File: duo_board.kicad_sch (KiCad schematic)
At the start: 24 parts, among them J1 TRRS, J2 2171790001, J3 Conn_01x04_Pin, U1 STM32F103C8Tx, U3 AMS1117-3.3, Y1 16Mhz

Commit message: routed, ready for production?
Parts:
- C1, C2, C3, C4, C8: value 100n -> 100nF; footprint (none) -> Capacitor_THT:C_Disc_D4.3mm_W1.9mm_P5.00mm
- C10, C9: value 20pF -> 22pF; footprint (none) -> Capacitor_THT:C_Disc_D3.0mm_W1.6mm_P2.50mm
- C11, C12: footprint (none) -> Capacitor_THT:C_Disc_D4.3mm_W1.9mm_P5.00mm
- C5: value 10u -> 10uF; footprint (none) -> Capacitor_THT:CP_Radial_Tantal_D5.5mm_P2.50mm
- C6: value 10n -> 10nF; footprint (none) -> Capacitor_THT:C_Disc_D4.3mm_W1.9mm_P5.00mm
- C7: value 1u -> 1uF; footprint (none) -> Capacitor_THT:C_Disc_D4.3mm_W1.9mm_P5.00mm
- R1, R2: footprint (none) -> Resistor_THT:R_Axial_DIN0207_L6.3mm_D2.5mm_P10.16mm_Horizontal
- Y1: footprint (none) -> Crystal:Crystal_HC49-4H_Vertical
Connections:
- net +3.3V: now also J1.6, J1.7, U2.H3 (H-), U2.V1 (V+)
- net GND: now also C10.2, C9.1, J1.5, U2.B2A (SEL-), U2.H1 (H+), U2.S1 (SHIELD), U2.S2 (SHIELD), U2.S3 (SHIELD), U2.S4 (SHIELD), U2.V3 (V-)
- net HSE_IN: now also C9.2, Y1.1; no longer C9.1
- net HSE_OUT: now also Y1.2
- net USART1_RX: now reaches J1.2
- net USART1_RX: now also U1.31 (PA10)
- net USART1_TX: now reaches J1.3
- net USART1_TX: now also J1.4, U1.30 (PA9)
- net X_AXIS: now reaches U1.18 (PB0)
- net X_AXIS: now also U2.V2 (V)
- net Y_AXIS: now reaches U1.19 (PB1)
- net Y_AXIS: now also U2.H2 (H)
- net BTN_PIN: now reaches U1.28 (PB15)
- net BTN_PIN: now also U2.B1A (SEL+)
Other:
- note added: "TEST POINTS"
- moved on the sheet: C1, C10, C9, J1, TP1, TP2, Y1

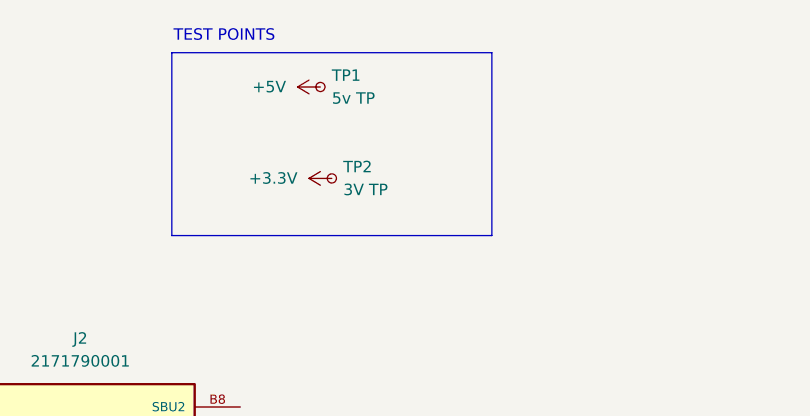
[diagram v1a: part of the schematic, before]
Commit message: added firmware submodule and updated pcb
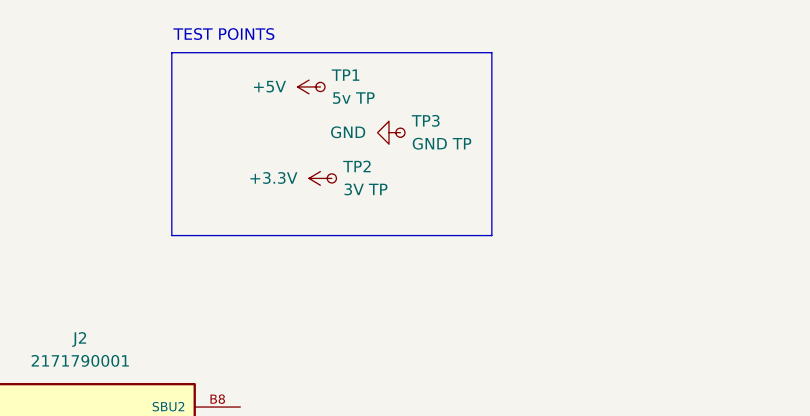
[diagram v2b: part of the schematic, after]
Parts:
- added TP3: GND TP, TestPoint:TestPoint_Pad_1.0x1.0mm, symbol Connector:TestPoint_Small
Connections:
- net GND: now also TP3.1
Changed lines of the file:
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@@
+	)
+	(symbol
+		(lib_id "Connector:TestPoint_Small")
+		(at 193.04 30.48 0)
+		(unit 1)
+		(exclude_from_sim no)
+		(in_bom yes)
+		(on_board yes)
+		(dnp no)
+		(fields_autoplaced yes)
+		(property "Reference" "TP3"
+			(at 194.31 29.2099 0)
+			(effects
+				(font
+					(size 1.27 1.27)
+				)
+				(justify left)
+			)
+		)
+		(property "Value" "GND TP"
+			(at 194.31 31.7499 0)
+			(effects
+				(font
+					(size 1.27 1.27)
+				)
+				(justify left)
+			)
+		)
+		(property "Footprint" "TestPoint:TestPoint_Pad_1.0x1.0mm"
+			(at 198.12 30.48 0)
+			(effects
+				(font
+					(size 1.27 1.27)
+				)
+				(hide yes)
+			)
+		)
+		(property "Datasheet" "~"
+			(at 198.12 30.48 0)
+			(effects
+				(font
+					(size 1.27 1.27)
+				)
+				(hide yes)
+			)
+		)
+		(property "Description" "test point"
+			(at 193.04 30.48 0)
+			(effects
+				(font
+					(size 1.27 1.27)
+				)
+				(hide yes)
+			)
+		)
+		(pin "1"
+		)
+		(instances
+			(project "duo_board"
+				(path "/05cf081a-bd8c-4d9b-9912-04c062082d45"
+					(reference "TP3")
+					(unit 1)
+				)
+			)
+		)
 	)
 	(symbol
@@
 					(unit 1)
 				)
+			)
+		)
+	)
+	(symbol
+		(lib_id "power:GND")
+		(at 193.04 30.48 270)
+		(unit 1)
+		(exclude_from_sim no)
+		(in_bom yes)
+		(on_board yes)
+		(dnp no)
+		(fields_autoplaced yes)
+		(property "Reference" "#PWR028"
+			(at 186.69 30.48 0)
+			(effects
+				(font
+					(size 1.27 1.27)
+				)
+				(hide yes)
+			)
+		)
+		(property "Value" "GND"
+			(at 189.23 30.4799 90)
+			(effects
+				(font
+					(size 1.27 1.27)
+				)
+				(justify right)
+			)
+		)
+		(property "Footprint" ""
+			(at 193.04 30.48 0)
+			(effects
+				(font
+					(size 1.27 1.27)
+				)
+				(hide yes)
+			)
+		)
+		(property "Datasheet" ""
+			(at 193.04 30.48 0)
+			(effects
+				(font
+					(size 1.27 1.27)
+				)
+				(hide yes)
+			)
+		)
+		(property "Description" "Power symbol creates a global label with name \"GND\" , ground"
+			(at 193.04 30.48 0)
+			(effects
+				(font
+					(size 1.27 1.27)
+				)
+				(hide yes)
+			)
+		)
+		(pin "1"
+		)
+		(instances
+			(project "duo_board"
+				(path "/05cf081a-bd8c-4d9b-9912-04c062082d45"
+					(reference "#PWR028")
+					(unit 1)
+				)
